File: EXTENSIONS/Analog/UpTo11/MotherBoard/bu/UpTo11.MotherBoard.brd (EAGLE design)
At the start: 68 x 58 mm, 9 parts, among them X1 USB-A

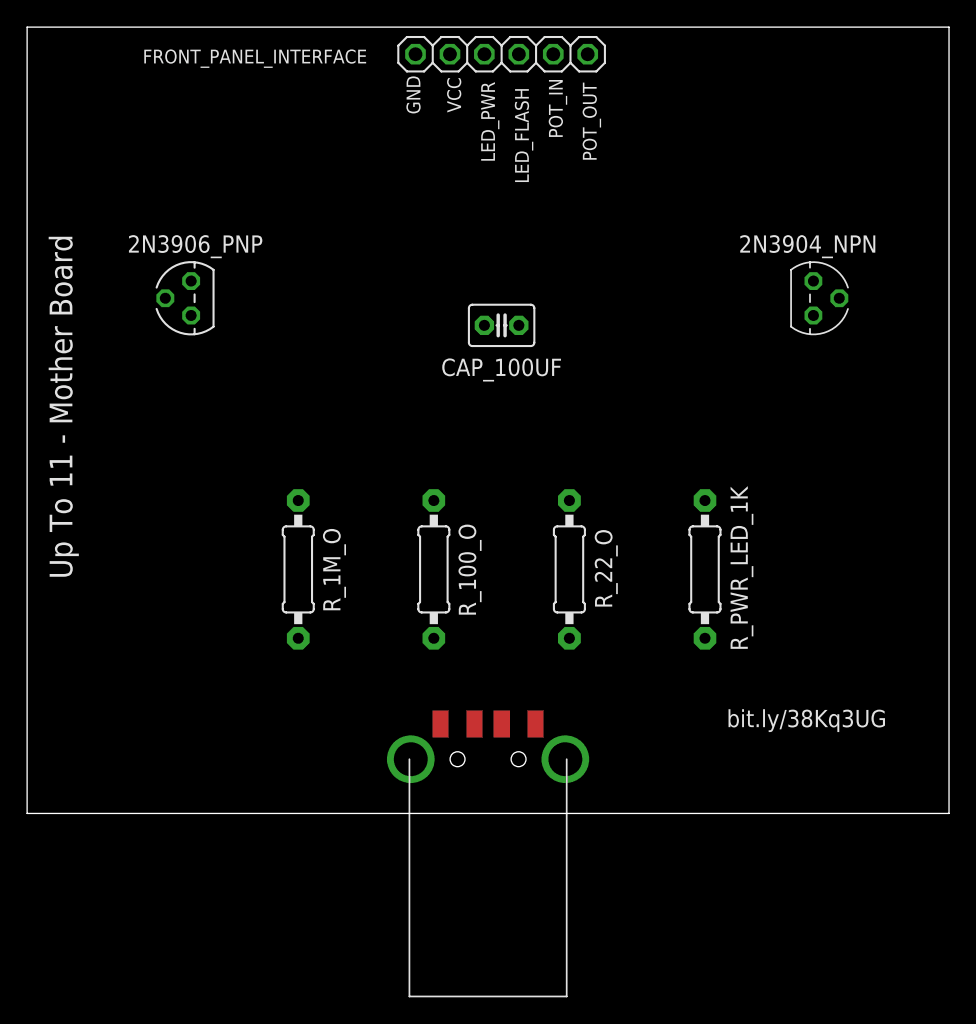
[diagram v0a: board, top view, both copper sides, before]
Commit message: Create UpTo11 Front Panel
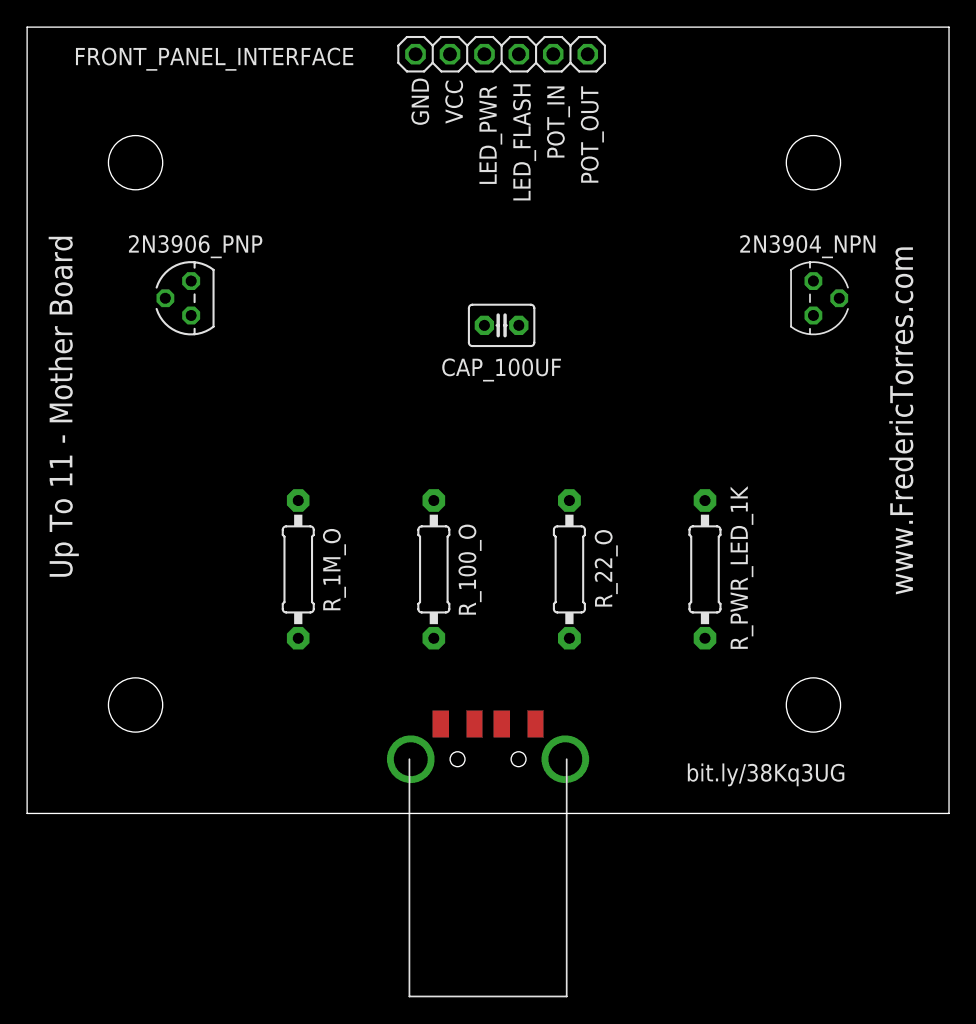
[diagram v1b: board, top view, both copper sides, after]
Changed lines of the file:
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@@
 <layer number="43" name="vRestrict" color="2" fill="10" visible="yes" active="yes"/>
 <layer number="44" name="Drills" color="7" fill="1" visible="no" active="yes"/>
-<layer number="45" name="Holes" color="7" fill="1" visible="no" active="yes"/>
+<layer number="45" name="Holes" color="7" fill="1" visible="yes" active="yes"/>
 <layer number="46" name="Milling" color="3" fill="1" visible="no" active="yes"/>
 <layer number="47" name="Measures" color="7" fill="1" visible="no" active="yes"/>
@@
 <text x="38.5" y="43" size="2.1844" layer="26" rot="MR0" align="center">MadeInTheUSB.net</text>
 <text x="4.5" y="21" size="1.27" layer="26" rot="MR90" align="center">PCBv1 - 2019.12</text>
-<text x="38" y="63" size="2.1844" layer="26" rot="MR0" align="center">Up To 11 - MotherBoard</text>
+<text x="36" y="63" size="2.1844" layer="26" rot="MR0" align="center">Up To 11 - MotherBoard</text>
 <text x="67.5" y="40" size="1.778" layer="26" rot="MR270" align="center">www.FredericTorres.com</text>
 <text x="36" y="56" size="1.6764" layer="26" rot="MR0" align="center">https://bit.ly/38Kq3UG</text>
-<text x="59.5" y="19" size="1.27" layer="25" align="center">bit.ly/38Kq3UG</text>
-<text x="30.5" y="65" size="1.016" layer="25" rot="R90" align="center">GND</text>
-<text x="33.5" y="65" size="1.016" layer="25" rot="R90" align="center">VCC</text>
-<text x="36" y="63" size="1.016" layer="25" rot="R90" align="center">LED_PWR</text>
-<text x="38.5" y="62" size="1.016" layer="25" rot="R90" align="center">LED_FLASH</text>
-<text x="41" y="64" size="1.016" layer="25" rot="R90" align="center">POT_IN</text>
-<text x="43.5" y="63" size="1.016" layer="25" rot="R90" align="center">POT_OUT</text>
+<text x="56.5" y="15" size="1.27" layer="25" align="center">bit.ly/38Kq3UG</text>
+<text x="31" y="64.5" size="1.27" layer="25" rot="R90" align="center">GND</text>
+<text x="33.5" y="64.5" size="1.27" layer="25" rot="R90" align="center">VCC</text>
+<text x="36" y="62" size="1.27" layer="25" rot="R90" align="center">LED_PWR</text>
+<text x="38.5" y="61.5" size="1.27" layer="25" rot="R90" align="center">LED_FLASH</text>
+<text x="41" y="63" size="1.27" layer="25" rot="R90" align="center">POT_IN</text>
+<text x="43.5" y="62" size="1.27" layer="25" rot="R90" align="center">POT_OUT</text>
+<hole x="10" y="60" drill="4"/>
+<hole x="10" y="20" drill="4"/>
+<hole x="60" y="60" drill="4"/>
+<hole x="60" y="20" drill="4"/>
+<text x="66.5" y="41" size="1.6764" layer="25" rot="R270" align="center">www.FredericTorres.com</text>
 </plain>
 <attributes>
@@
 </element>
 <element name="FRONT_PANEL_INTERFACE" library="adafruit" package="1X06" value="" x="37" y="68" smashed="yes">
-<attribute name="NAME" x="18.8038" y="67.8288" size="1.016" layer="25" ratio="10" align="center"/>
+<attribute name="NAME" x="15.8038" y="67.8288" size="1.27" layer="25" ratio="10" align="center"/>
 <attribute name="VALUE" x="29.38" y="64.825" size="1.27" layer="27"/>
 </element>

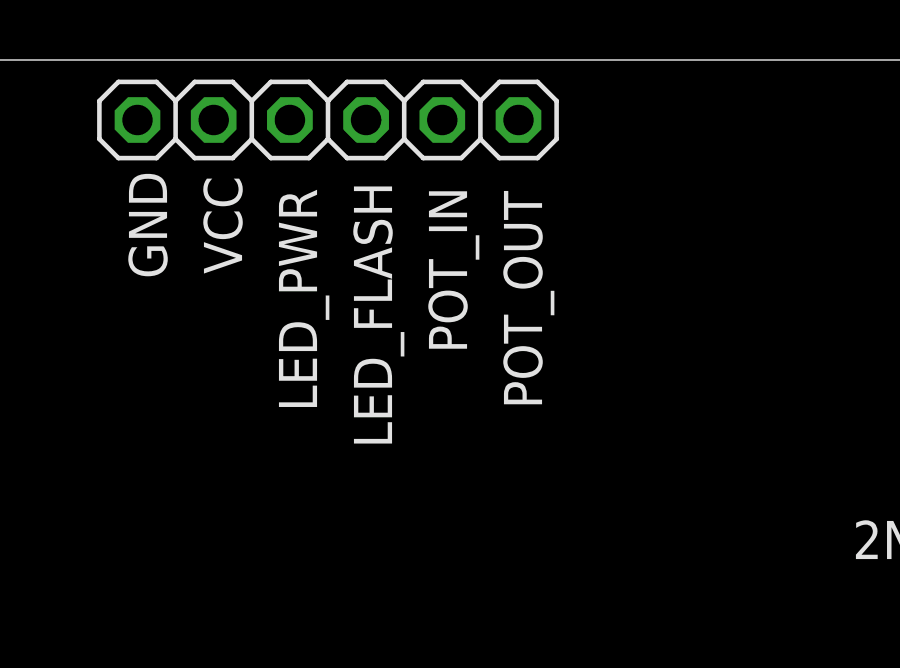
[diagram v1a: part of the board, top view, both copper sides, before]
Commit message: Create UpTo11 Front Panel
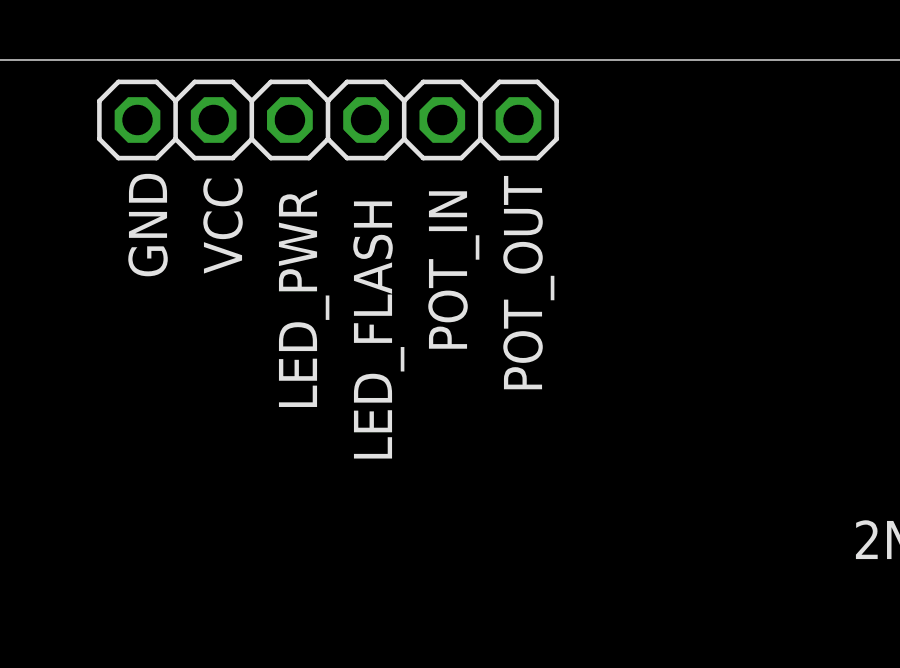
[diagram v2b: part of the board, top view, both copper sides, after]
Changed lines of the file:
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@@
 <text x="33.5" y="64.5" size="1.27" layer="25" rot="R90" align="center">VCC</text>
 <text x="36" y="62" size="1.27" layer="25" rot="R90" align="center">LED_PWR</text>
-<text x="38.5" y="61.5" size="1.27" layer="25" rot="R90" align="center">LED_FLASH</text>
+<text x="38.5" y="61" size="1.27" layer="25" rot="R90" align="center">LED_FLASH</text>
 <text x="41" y="63" size="1.27" layer="25" rot="R90" align="center">POT_IN</text>
-<text x="43.5" y="62" size="1.27" layer="25" rot="R90" align="center">POT_OUT</text>
+<text x="43.5" y="62.5" size="1.27" layer="25" rot="R90" align="center">POT_OUT</text>
 <hole x="10" y="60" drill="4"/>
 <hole x="10" y="20" drill="4"/>

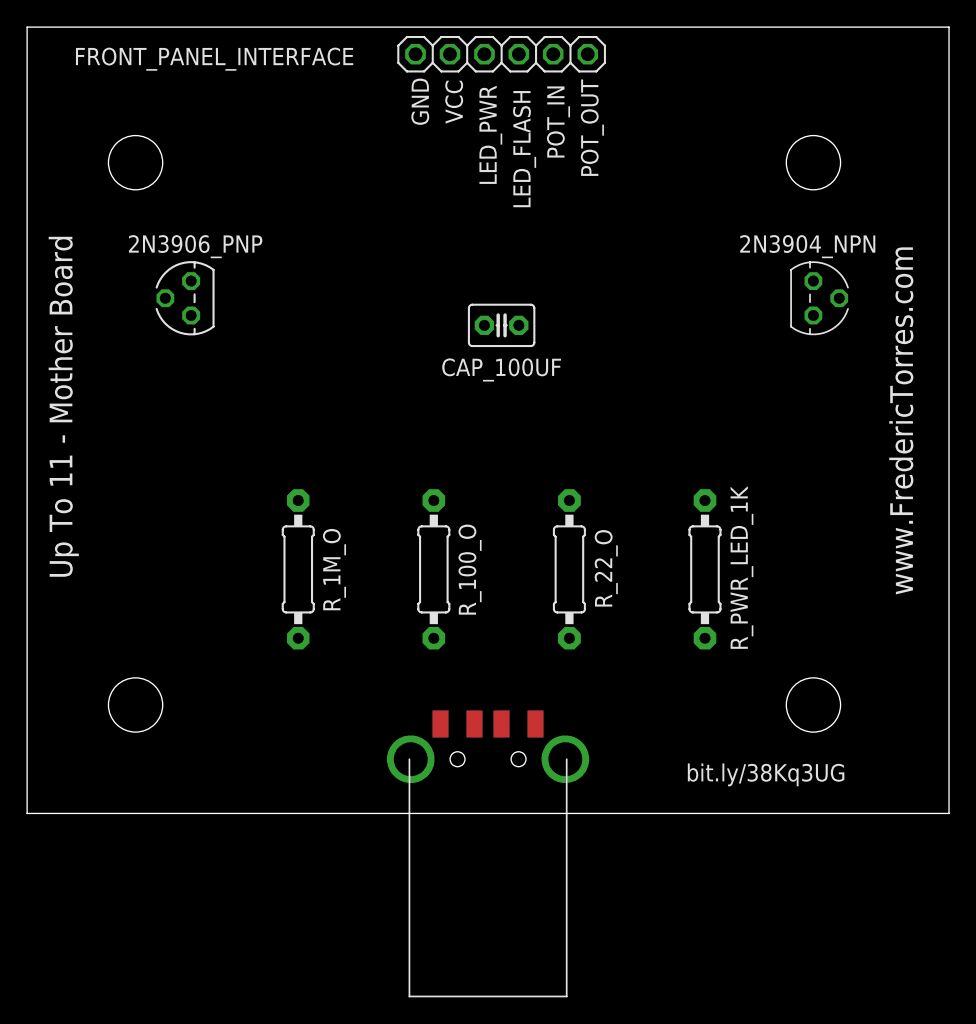
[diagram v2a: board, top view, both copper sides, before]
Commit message: Create UpTo11 Front Panel
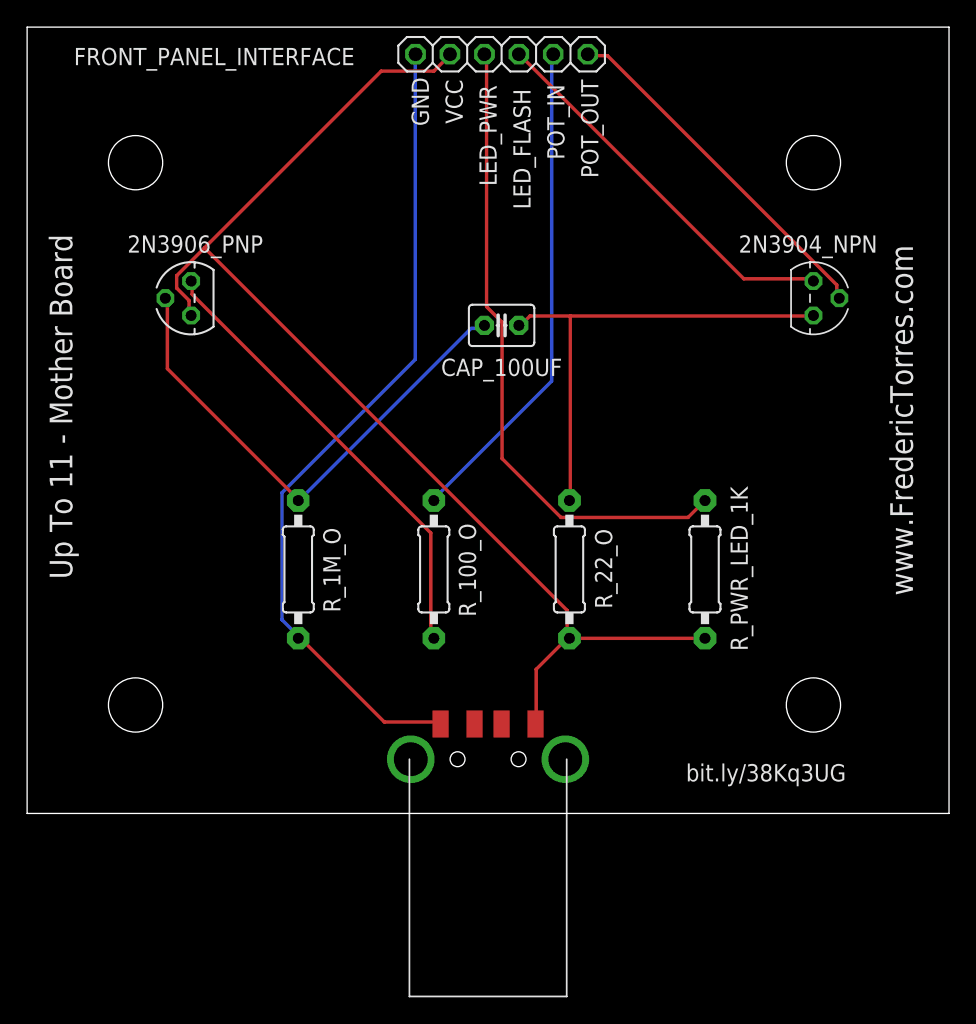
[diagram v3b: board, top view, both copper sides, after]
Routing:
- net VCC: track 0.00 -> 87.7 mm
- net GND_EX: track 0.00 -> 60.8 mm
- net LED_PWR: track 0.00 -> 47.7 mm
- net N$5: track 0.00 -> 38.1 mm
- net POT_IN: track 0.00 -> 36.6 mm
- net N$2: track 0.00 -> 35.6 mm
- net N$6: track 0.00 -> 33.8 mm
- net LED_FLASH: track 0.00 -> 28.7 mm
- net POT_OUT: track 0.00 -> 26.5 mm
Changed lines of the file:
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@@
 <contactref element="2N3904_NPN" pad="1"/>
 <contactref element="CAP_100UF" pad="2"/>
-<wire x1="42" y1="35.08" x2="60" y2="48.73" width="0" layer="19" extent="1-1"/>
-<wire x1="38.27" y1="48" x2="42" y2="35.08" width="0" layer="19" extent="1-1"/>
+<wire x1="39.0906" y1="48.6918" x2="42.0624" y2="48.6918" width="0.254" layer="1"/>
+<wire x1="42.0624" y1="48.6918" x2="59.8932" y2="48.6918" width="0.254" layer="1"/>
+<wire x1="38.4048" y1="48.006" x2="39.0906" y2="48.6918" width="0.254" layer="1"/>
+<wire x1="59.8932" y1="48.6918" x2="60" y2="48.73" width="0.254" layer="1"/>
+<wire x1="38.4048" y1="48.006" x2="38.27" y2="48" width="0.254" layer="1"/>
+<wire x1="42.0624" y1="48.6918" x2="42.0624" y2="35.2044" width="0.254" layer="1"/>
+<wire x1="42.0624" y1="35.2044" x2="42" y2="35.08" width="0.254" layer="1"/>
 </signal>
 <signal name="LED_FLASH">
 <contactref element="2N3904_NPN" pad="3"/>
 <contactref element="FRONT_PANEL_INTERFACE" pad="4"/>
-<wire x1="38.27" y1="68" x2="60" y2="51.27" width="0" layer="19" extent="1-1"/>
+<wire x1="54.864" y1="51.435" x2="59.8932" y2="51.435" width="0.254" layer="1"/>
+<wire x1="38.4048" y1="67.8942" x2="54.864" y2="51.435" width="0.254" layer="1"/>
+<wire x1="59.8932" y1="51.435" x2="60" y2="51.27" width="0.254" layer="1"/>
+<wire x1="38.4048" y1="67.8942" x2="38.27" y2="68" width="0.254" layer="1"/>
 </signal>
 <signal name="GND_EX">
@@
 <contactref element="R_1M_O" pad="1"/>
 <contactref element="FRONT_PANEL_INTERFACE" pad="1"/>
-<wire x1="22" y1="24.92" x2="30.65" y2="68" width="0" layer="19" extent="1-1"/>
-<wire x1="32.5" y1="18.6" x2="22" y2="24.92" width="0" layer="19" extent="1-1"/>
+<wire x1="28.3464" y1="18.7452" x2="32.4612" y2="18.7452" width="0.254" layer="1"/>
+<wire x1="22.1742" y1="24.9174" x2="28.3464" y2="18.7452" width="0.254" layer="1"/>
+<wire x1="32.4612" y1="18.7452" x2="32.5" y2="18.6" width="0.254" layer="1"/>
+<wire x1="22.1742" y1="24.9174" x2="22" y2="24.92" width="0.254" layer="1"/>
+<wire x1="30.6324" y1="45.4914" x2="30.6324" y2="67.8942" width="0.254" layer="16"/>
+<wire x1="20.8026" y1="35.6616" x2="30.6324" y2="45.4914" width="0.254" layer="16"/>
+<wire x1="20.8026" y1="26.289" x2="20.8026" y2="35.6616" width="0.254" layer="16"/>
+<wire x1="21.9456" y1="25.146" x2="20.8026" y2="26.289" width="0.254" layer="16"/>
+<wire x1="30.6324" y1="67.8942" x2="30.65" y2="68" width="0.254" layer="16"/>
+<wire x1="21.9456" y1="25.146" x2="22" y2="24.92" width="0.254" layer="16"/>
 </signal>
 <signal name="N$5">
@@
 <contactref element="2N3906_PNP" pad="2"/>
 <contactref element="R_1M_O" pad="2"/>
-<wire x1="12.195" y1="50" x2="35.73" y2="48" width="0" layer="19" extent="1-1"/>
-<wire x1="22" y1="35.08" x2="12.195" y2="50" width="0" layer="19" extent="1-1"/>
+<wire x1="12.3444" y1="44.8056" x2="12.3444" y2="49.8348" width="0.254" layer="1"/>
+<wire x1="21.9456" y1="35.2044" x2="12.3444" y2="44.8056" width="0.254" layer="1"/>
+<wire x1="12.3444" y1="49.8348" x2="12.195" y2="50" width="0.254" layer="1"/>
+<wire x1="21.9456" y1="35.2044" x2="22" y2="35.08" width="0.254" layer="1"/>
+<wire x1="34.7472" y1="47.7774" x2="35.6616" y2="47.7774" width="0.254" layer="16"/>
+<wire x1="22.1742" y1="35.2044" x2="34.7472" y2="47.7774" width="0.254" layer="16"/>
+<wire x1="35.6616" y1="47.7774" x2="35.73" y2="48" width="0.254" layer="16"/>
+<wire x1="22.1742" y1="35.2044" x2="22" y2="35.08" width="0.254" layer="16"/>
 </signal>
 <signal name="N$6">
 <contactref element="2N3906_PNP" pad="1"/>
 <contactref element="R_100_O" pad="1"/>
-<wire x1="32" y1="24.92" x2="14.1" y2="51.27" width="0" layer="19" extent="1-1"/>
+<wire x1="14.1732" y1="50.292" x2="14.1732" y2="51.2064" width="0.254" layer="1"/>
+<wire x1="31.7754" y1="32.6898" x2="14.1732" y2="50.292" width="0.254" layer="1"/>
+<wire x1="31.7754" y1="25.146" x2="31.7754" y2="32.6898" width="0.254" layer="1"/>
+<wire x1="14.1732" y1="51.2064" x2="14.1" y2="51.27" width="0.254" layer="1"/>
+<wire x1="31.7754" y1="25.146" x2="32" y2="24.92" width="0.254" layer="1"/>
 </signal>
 <signal name="VCC">
@@
 <contactref element="2N3906_PNP" pad="3"/>
 <contactref element="R_PWR_LED_1K" pad="2"/>
-<wire x1="14.1" y1="48.73" x2="33.19" y2="68" width="0" layer="19" extent="1-1"/>
-<wire x1="39.5" y1="18.6" x2="14.1" y2="48.73" width="0" layer="19" extent="1-1"/>
-<wire x1="42" y1="24.92" x2="39.5" y2="18.6" width="0" layer="19" extent="1-1"/>
-<wire x1="52" y1="24.92" x2="42" y2="24.92" width="0" layer="19" extent="1-1"/>
+<wire x1="39.5478" y1="22.6314" x2="39.5478" y2="18.7452" width="0.254" layer="1"/>
+<wire x1="41.8338" y1="24.9174" x2="39.5478" y2="22.6314" width="0.254" layer="1"/>
+<wire x1="39.5478" y1="18.7452" x2="39.5" y2="18.6" width="0.254" layer="1"/>
+<wire x1="41.8338" y1="24.9174" x2="42" y2="24.92" width="0.254" layer="1"/>
+<wire x1="42.0624" y1="24.9174" x2="51.8922" y2="24.9174" width="0.254" layer="1"/>
+<wire x1="51.8922" y1="24.9174" x2="52" y2="24.92" width="0.254" layer="1"/>
+<wire x1="42.0624" y1="24.9174" x2="42" y2="24.92" width="0.254" layer="1"/>
+<wire x1="13.9446" y1="49.8348" x2="13.9446" y2="48.9204" width="0.254" layer="1"/>
+<wire x1="13.0302" y1="50.7492" x2="13.9446" y2="49.8348" width="0.254" layer="1"/>
+<wire x1="13.0302" y1="51.6636" x2="13.0302" y2="50.7492" width="0.254" layer="1"/>
+<wire x1="28.1178" y1="66.7512" x2="15.0876" y2="53.721" width="0.254" layer="1"/>
+<wire x1="15.0876" y1="53.721" x2="13.0302" y2="51.6636" width="0.254" layer="1"/>
+<wire x1="32.004" y1="66.7512" x2="28.1178" y2="66.7512" width="0.254" layer="1"/>
+<wire x1="33.147" y1="67.8942" x2="32.004" y2="66.7512" width="0.254" layer="1"/>
+<wire x1="13.9446" y1="48.9204" x2="14.1" y2="48.73" width="0.254" layer="1"/>
+<wire x1="33.147" y1="67.8942" x2="33.19" y2="68" width="0.254" layer="1"/>
+<wire x1="41.8338" y1="26.9748" x2="41.8338" y2="25.146" width="0.254" layer="1"/>
+<wire x1="15.0876" y1="53.721" x2="41.8338" y2="26.9748" width="0.254" layer="1"/>
+<wire x1="41.8338" y1="25.146" x2="42" y2="24.92" width="0.254" layer="1"/>
 </signal>
 <signal name="LED_PWR">
 <contactref element="R_PWR_LED_1K" pad="1"/>
 <contactref element="FRONT_PANEL_INTERFACE" pad="3"/>
-<wire x1="35.73" y1="68" x2="52" y2="35.08" width="0" layer="19" extent="1-1"/>
+<wire x1="35.8902" y1="49.3776" x2="35.8902" y2="67.8942" width="0.254" layer="1"/>
+<wire x1="37.0332" y1="48.2346" x2="35.8902" y2="49.3776" width="0.254" layer="1"/>
+<wire x1="37.0332" y1="38.1762" x2="37.0332" y2="48.2346" width="0.254" layer="1"/>
+<wire x1="41.3766" y1="33.8328" x2="37.0332" y2="38.1762" width="0.254" layer="1"/>
+<wire x1="50.7492" y1="33.8328" x2="41.3766" y2="33.8328" width="0.254" layer="1"/>
+<wire x1="51.8922" y1="34.9758" x2="50.7492" y2="33.8328" width="0.254" layer="1"/>
+<wire x1="35.8902" y1="67.8942" x2="35.73" y2="68" width="0.254" layer="1"/>
+<wire x1="51.8922" y1="34.9758" x2="52" y2="35.08" width="0.254" layer="1"/>
 </signal>
 <signal name="POT_IN">
 <contactref element="R_100_O" pad="2"/>
 <contactref element="FRONT_PANEL_INTERFACE" pad="5"/>
-<wire x1="32" y1="35.08" x2="40.81" y2="68" width="0" layer="19" extent="1-1"/>
+<wire x1="40.6908" y1="43.8912" x2="40.6908" y2="67.8942" width="0.254" layer="16"/>
+<wire x1="32.004" y1="35.2044" x2="40.6908" y2="43.8912" width="0.254" layer="16"/>
+<wire x1="40.6908" y1="67.8942" x2="40.81" y2="68" width="0.254" layer="16"/>
+<wire x1="32.004" y1="35.2044" x2="32" y2="35.08" width="0.254" layer="16"/>
 </signal>
 <signal name="POT_OUT">
 <contactref element="2N3904_NPN" pad="2"/>
 <contactref element="FRONT_PANEL_INTERFACE" pad="6"/>
-<wire x1="43.35" y1="68" x2="61.905" y2="50" width="0" layer="19" extent="1-1"/>
+<wire x1="61.722" y1="50.9778" x2="61.722" y2="50.0634" width="0.254" layer="1"/>
+<wire x1="44.8056" y1="67.8942" x2="61.722" y2="50.9778" width="0.254" layer="1"/>
+<wire x1="43.434" y1="67.8942" x2="44.8056" y2="67.8942" width="0.254" layer="1"/>
+<wire x1="61.722" y1="50.0634" x2="61.905" y2="50" width="0.254" layer="1"/>
+<wire x1="43.434" y1="67.8942" x2="43.35" y2="68" width="0.254" layer="1"/>
 </signal>
 </signals>
